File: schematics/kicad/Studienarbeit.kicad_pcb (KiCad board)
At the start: 2 copper layers, 73 x 73 mm, 72 parts, among them J1 AudioJack3, J2 Conn_01x18, J3 Conn_01x18, J4 Conn_01x01_Pin, J5 Conn_01x01_Pin, J6 Conn_01x01_Pin, J7 Conn_01x01_Pin, U2 PCM5102, U3 MCP6001-OT, U4 MCP6001-OT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

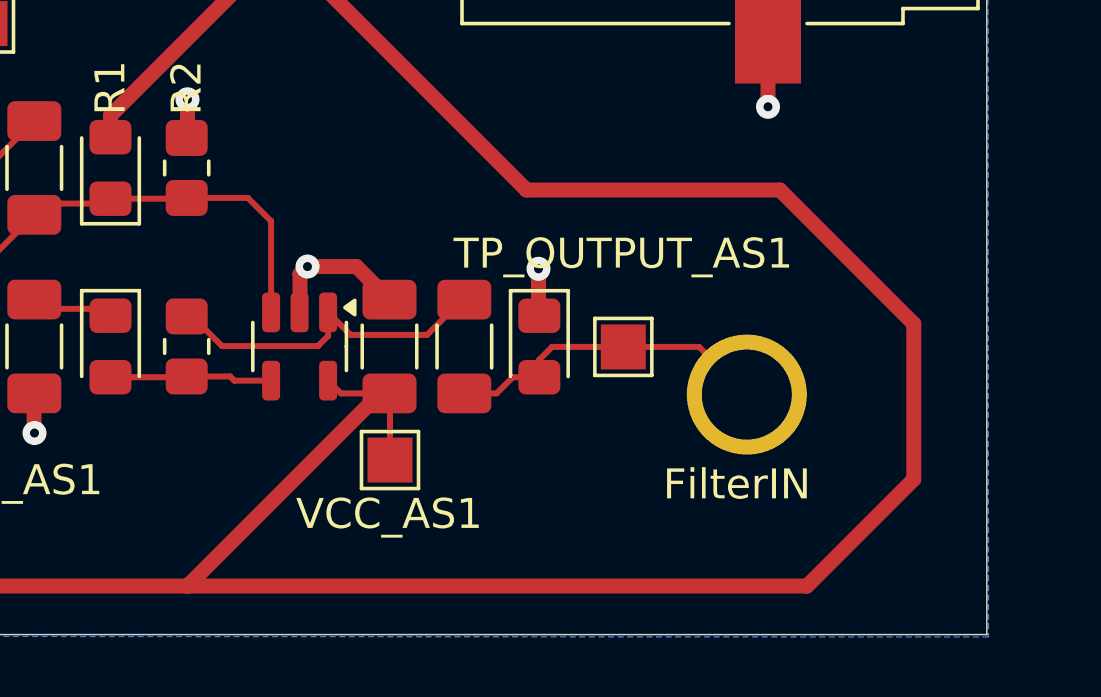
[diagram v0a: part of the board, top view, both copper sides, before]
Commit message: KiCad: Added jumper wires and resistors for gain control.
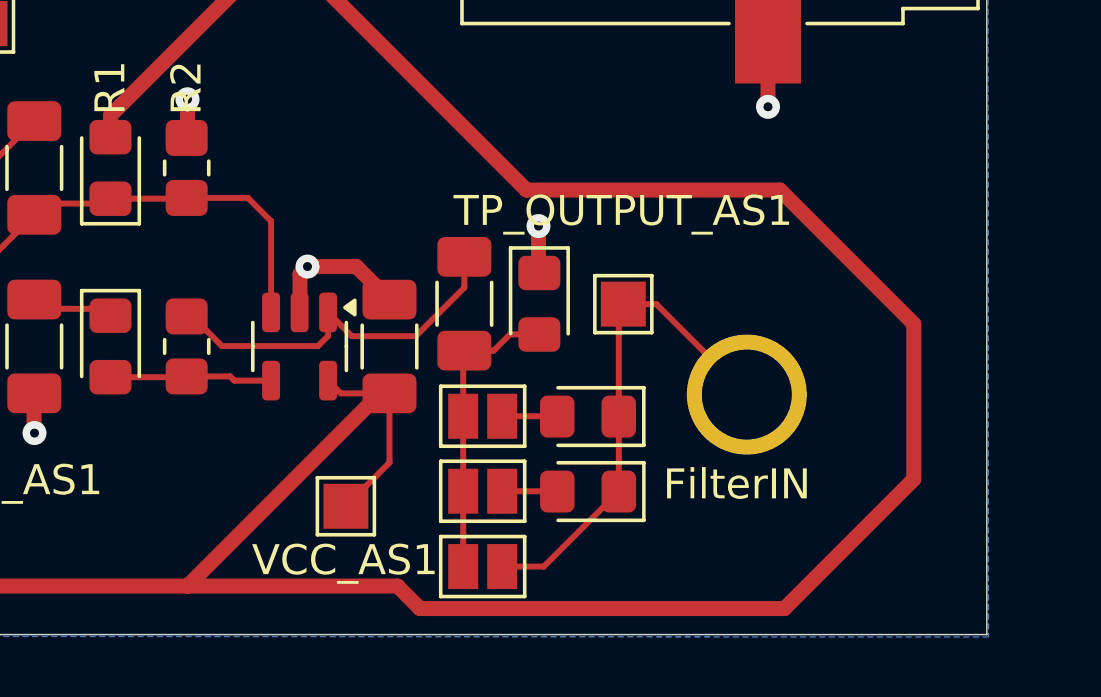
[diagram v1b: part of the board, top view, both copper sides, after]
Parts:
- added JP1: Jumper_2_Open, Jumper:SolderJumper-2_P1.3mm_Open_Pad1.0x1.5mm, F.Cu at (263.8, 104.3)
- added JP2: Jumper_2_Open, Jumper:SolderJumper-2_P1.3mm_Open_Pad1.0x1.5mm, F.Cu at (263.8, 101.8)
- added JP3: Jumper_2_Open, Jumper:SolderJumper-2_P1.3mm_Open_Pad1.0x1.5mm, F.Cu at (263.8, 106.8)
- added R_COUPLING_AMPSTAGE2: 10K, LED_SMD:LED_0805_2012Metric_Pad1.15x1.40mm_HandSolder, F.Cu at (267.3, 104.3)
- added R_COUPLING_AMPSTAGE3: 1K, LED_SMD:LED_0805_2012Metric_Pad1.15x1.40mm_HandSolder, F.Cu at (267.3, 101.8)
- moved VCC_AS1 2.13 mm to (259.2, 104.8)
- moved C_COUPLING_AMPSTAGE1 1.42 mm to (263.2, 98.0)
- moved R_COUPLING_AMPSTAGE1 1.42 mm to (265.7, 98.0)
- moved TP_OUTPUT_AS1 1.42 mm to (268.5, 98.1)
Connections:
- C_COUPLING_AMPSTAGE1 pad 1: /ES2FILTER -> Net-(JP1-A)
- R_COUPLING_AMPSTAGE1 pad 2: /ES2FILTER -> Net-(JP1-A)
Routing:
- net Net-(JP1-A): track 0.00 -> 9.60 mm
- net /ES2FILTER: track 38.3 -> 44.8 mm
- net +5V: track 323.1 -> 325.9 mm
- net Net-(JP1-B): track 0.00 -> 1.84 mm
- net Net-(JP2-B): track 0.00 -> 1.84 mm
- net Net-(C_COUPLING_AMPSTAGE1-Pad2): track 11.3 -> 12.6 mm

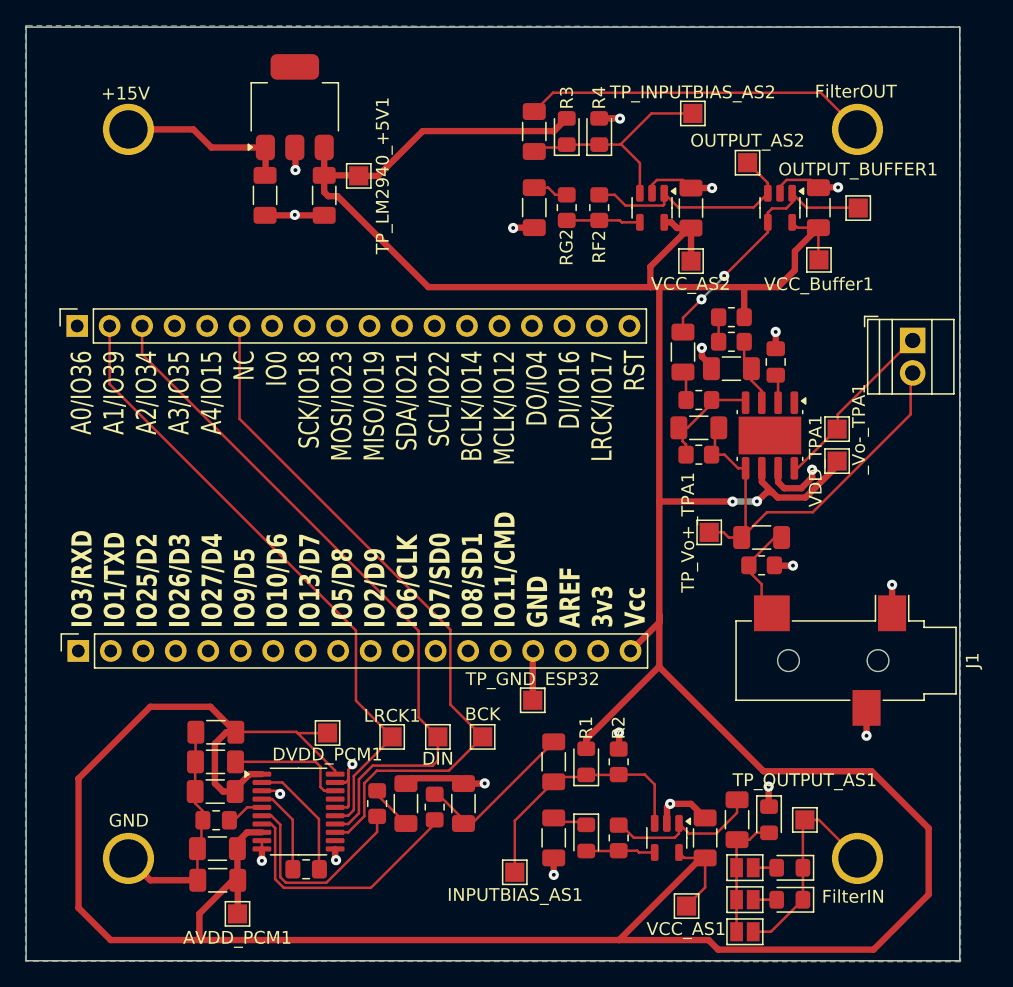
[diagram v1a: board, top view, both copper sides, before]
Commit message: Updated PCB based on feedback (1).
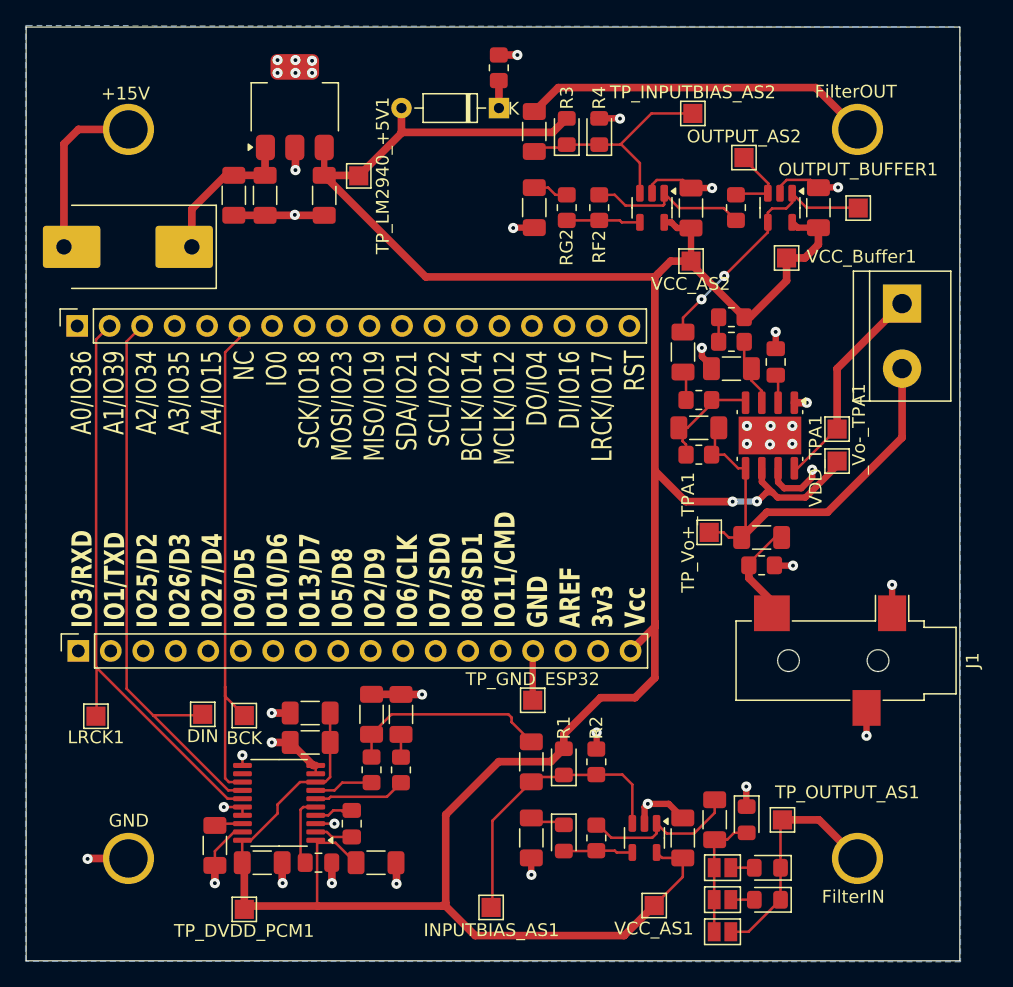
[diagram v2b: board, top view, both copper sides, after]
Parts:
- removed AVDD_PCM1: TestPoint, TestPoint:TestPoint_Pad_1.5x1.5mm
- added C_IN_+15V_1: 10uF, Capacitor_SMD:C_1206_3216Metric_Pad1.33x1.80mm_HandSolder, F.Cu at (223.8, 49.2)
- added D1: D_Schottky, Diode_SMD:D_SMC-RM10_Universal_Handsoldering, F.Cu at (215.6, 53.2)
- added D2: 1N4148, Diode_THT:D_DO-35_SOD27_P7.62mm_Horizontal, F.Cu at (244.6, 42.4)
- added DEBUG1: 0, Resistor_SMD:R_0805_2012Metric_Pad1.20x1.40mm_HandSolder, F.Cu at (263.1, 50.2)
- added STATUS_LED1: 330, Resistor_SMD:R_0805_2012Metric_Pad1.20x1.40mm_HandSolder, F.Cu at (244.6, 39.2)
- LS1: footprint TerminalBlock:TerminalBlock_Xinya_XY308-2.54-2P_1x02_P2.54mm_Horizontal -> TerminalBlock:TerminalBlock_bornier-2_P5.08mm
- moved LRCK1 23.2 mm to (213.1, 90.0), turned to 180 degrees
- moved BCK 18.7 mm to (224.7, 89.9), turned to 0 degrees
- moved DIN 18.5 mm to (221.4, 89.8)
- moved TP_DVDD_PCM1 15.2 mm to (224.7, 105.0)
- moved C1_APS_PCM5102 14.9 mm to (229.8, 89.7)
- moved C1_CPPS_PCM1 13.8 mm to (234.9, 101.4), turned to 180 degrees
- moved C2_APS_PCM5102 11.0 mm to (229.8, 92.0)
- moved C1_DPS_PCM1 10.8 mm to (226.1, 101.4), turned to 180 degrees
- moved CG2_PCM5102 10.0 mm to (234.6, 89.8)
- moved C2_CPPS_PCM1 8.66 mm to (230.4, 101.4), turned to 180 degrees
- moved CG1_PCM5102 6.98 mm to (236.9, 89.8)
- moved C2_DPS_PCM1 6.53 mm to (222.3, 100.0), turned to -90 degrees
- moved ROUTDACR1 5.73 mm to (234.6, 94.1)
- moved CA_PCM5102 5.04 mm to (233.1, 98.3), turned to 90 degrees
- moved INPUTBIAS_AS1 3.31 mm to (243.9, 104.9)
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- renumbered DVDD_PCM1 to TP_DVDD_PCM1
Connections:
- C_INPUT_LDO1 pad 2: +15V -> Net-(D1-K)
- C_IN_AMPSTAGE1 pad 1: /ES2FILTER -> /Filter_OUT
- J6 pad 1: /ES2FILTER -> /Filter_OUT
- J7 pad 1: /ES2FILTER -> /Filter_IN
- JP3 pad 2: /ES2FILTER -> /Filter_IN
- OUTPUT_AS2 pad 1: Net-(RF2-Pad2) -> Net-(DEBUG1-Pad2)
- RF2 pad 2: Net-(RF2-Pad2) -> Net-(DEBUG1-Pad1)
- R_COUPLING_AMPSTAGE2 pad 1: /ES2FILTER -> /Filter_IN
- R_COUPLING_AMPSTAGE3 pad 1: /ES2FILTER -> /Filter_IN
- TP_OUTPUT_AS1 pad 1: /ES2FILTER -> /Filter_IN
- U2 pad 12: /SCK -> unconnected-(U2-SCK-Pad12)
- U2 pad 17: /XSMT/MUTE -> GND
- U3 pad 1: Net-(RF2-Pad2) -> Net-(DEBUG1-Pad1)
- U5 pad 3: Net-(RF2-Pad2) -> Net-(DEBUG1-Pad2)
- U6 pad 1: /SYSTEMCTL -> GND
- U7 pad 1: +15V -> Net-(D1-K)
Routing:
- net +5V: track 325.9 -> 234.5 mm
- net /ES2FILTER: track 44.8 -> 0.00 mm
- net /Filter_OUT: track 0.00 -> 27.5 mm
- net /Filter_IN: track 0.00 -> 19.4 mm
- net Net-(RF2-Pad2): track 18.4 -> 0.00 mm
- net /BCK: track 56.1 -> 40.2 mm
- net Net-(U2-OUTR): track 20.3 -> 4.62 mm
- net Net-(DEBUG1-Pad1): track 0.00 -> 12.8 mm
- net Net-(D1-K): track 0.00 -> 12.0 mm
- net /DIN: track 55.2 -> 45.1 mm
- net Net-(U2-OUTL): track 16.4 -> 7.59 mm
- net /LDOO: track 9.62 -> 2.31 mm
- net Net-(U2-CAPP): track 9.59 -> 3.06 mm
- net Net-(DEBUG1-Pad2): track 0.00 -> 5.60 mm
- net GND: track 88.4 -> 84.7 mm, vias 21 -> 35
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
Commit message: Updated the PCB with prof feedback.
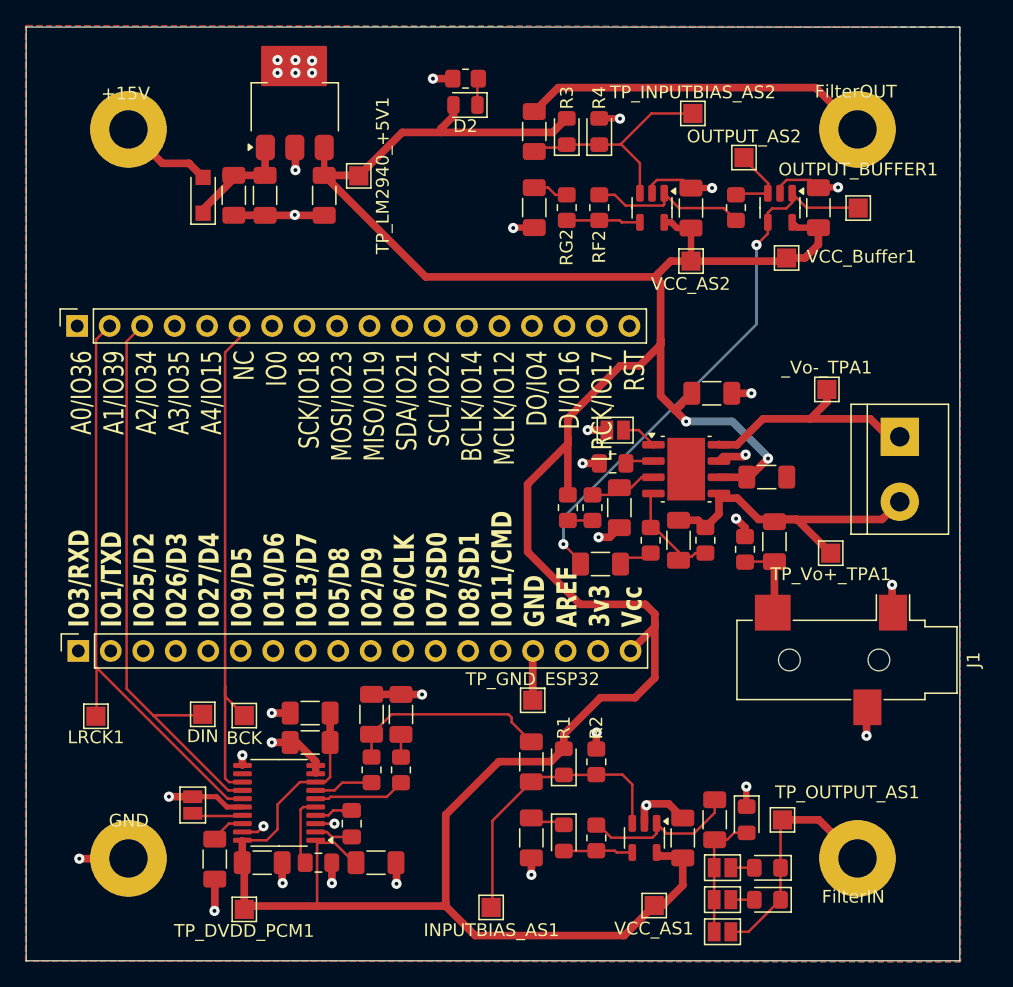
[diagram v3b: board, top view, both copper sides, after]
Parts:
- removed VDD_TPA1: TestPoint, TestPoint:TestPoint_Pad_1.5x1.5mm
- added C_INPUT_TPA1: 10uF, Capacitor_SMD:C_1206_3216Metric_Pad1.33x1.80mm_HandSolder, F.Cu at (265.5, 71.2)
- added C_INPUT_TPA2: 100nF, Capacitor_SMD:C_1206_3216Metric_Pad1.33x1.80mm_HandSolder, F.Cu at (261.2, 64.7)
- added JP4: Jumper_2_Open, Jumper:SolderJumper-2_P1.3mm_Open_Pad1.0x1.5mm, F.Cu at (220.6, 96.9)
- added JP5: Jumper_2_Open, Jumper:SolderJumper-2_P1.3mm_Open_Pad1.0x1.5mm, F.Cu at (253.7, 67.6)
- D1: footprint Diode_SMD:D_SMC-RM10_Universal_Handsoldering -> Diode_SMD:Nexperia_CFP3_SOD-123W
- D2: footprint Diode_THT:D_DO-35_SOD27_P7.62mm_Horizontal -> Diode_SMD:D_0805_2012Metric
- J4, J5, J6, J7: footprint TestPoint:TestPoint_THTPad_2.0x2.0mm_Drill1.0mm -> TestPoint:FestoBoard_Drill_Hole
- moved R12 19.6 mm to (249.9, 73.6), turned to 90 degrees
- moved CI_TPA711 17.8 mm to (252.5, 78.0), turned to 180 degrees
- moved R13 16.9 mm to (251.9, 73.6), turned to 90 degrees
- moved CB_TPA1 15.0 mm to (253.4, 70.2), turned to 180 degrees
- moved C_SE/BTL_TPA1 14.0 mm to (254.0, 73.6), turned to -90 degrees
- moved RI_TPA711 11.6 mm to (256.4, 76.2), turned to 90 degrees
- moved LS1 10.4 mm to (275.9, 68.1)
- moved TP_Vo+_TPA1 9.64 mm to (270.5, 77.2), turned to 180 degrees
- moved CF_TPA711 8.93 mm to (258.6, 76.2), turned to 90 degrees
- moved D1 7.13 mm to (221.4, 49.2), turned to 90 degrees
- moved U6 7.06 mm to (259.2, 70.6), turned to 0 degrees
- moved RF_TPA711 6.71 mm to (260.7, 76.2), turned to -90 degrees
- moved _Vo-_TPA1 3.20 mm to (270.2, 64.4), turned to 180 degrees
- moved STATUS_LED1 2.74 mm to (241.9, 40.1), turned to 0 degrees
- moved D2 2.63 mm to (241.9, 42.2)
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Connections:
- U2 pad 17: GND -> Net-(JP4-B)
- U6 pad 1: GND -> Net-(JP5-B)
- U7 pad 4: (no net) -> GND
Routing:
- net /BUFFEROUT: track 20.7 -> 43.2 mm
- net +5V: track 234.5 -> 250.2 mm
- net /Vo+: track 35.2 -> 25.6 mm
- net GND: track 84.7 -> 91.0 mm, vias 35 -> 37
- net +15V: track 13.6 -> 7.39 mm
- net Net-(JP4-B): track 0.00 -> 4.35 mm
- net /Vo-: track 16.6 -> 19.5 mm
- net Net-(JP5-B): track 0.00 -> 2.82 mm
- net Net-(D1-K): track 12.0 -> 9.31 mm
- net Net-(CC_TPA711-Pad2): track 10.4 -> 8.44 mm
- net unconnected-(U6-GND-Pad9): vias 6 -> 0
- added copper zone on F.Cu, net GND

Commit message: Updated the parts list.
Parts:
- D1: footprint Diode_SMD:Nexperia_CFP3_SOD-123W -> Diode_SMD:D_SOD-123F
- D2: footprint Diode_SMD:D_0805_2012Metric -> Diode_SMD:D_SOD-123F
- RF1, RF2: value 10K -> 5K
- RG1: value 200k -> 100k; footprint LED_SMD:LED_0805_2012Metric_Pad1.15x1.40mm_HandSolder -> Resistor_SMD:R_0805_2012Metric_Pad1.20x1.40mm_HandSolder
- RG2: value 200K -> 100K
- R_COUPLING_AMPSTAGE1: footprint LED_SMD:LED_0805_2012Metric_Pad1.15x1.40mm_HandSolder -> Resistor_SMD:R_0805_2012Metric_Pad1.20x1.40mm_HandSolder
- moved D2 0.14 mm to (241.8, 42.2)
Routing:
- net GND: vias 37 -> 38

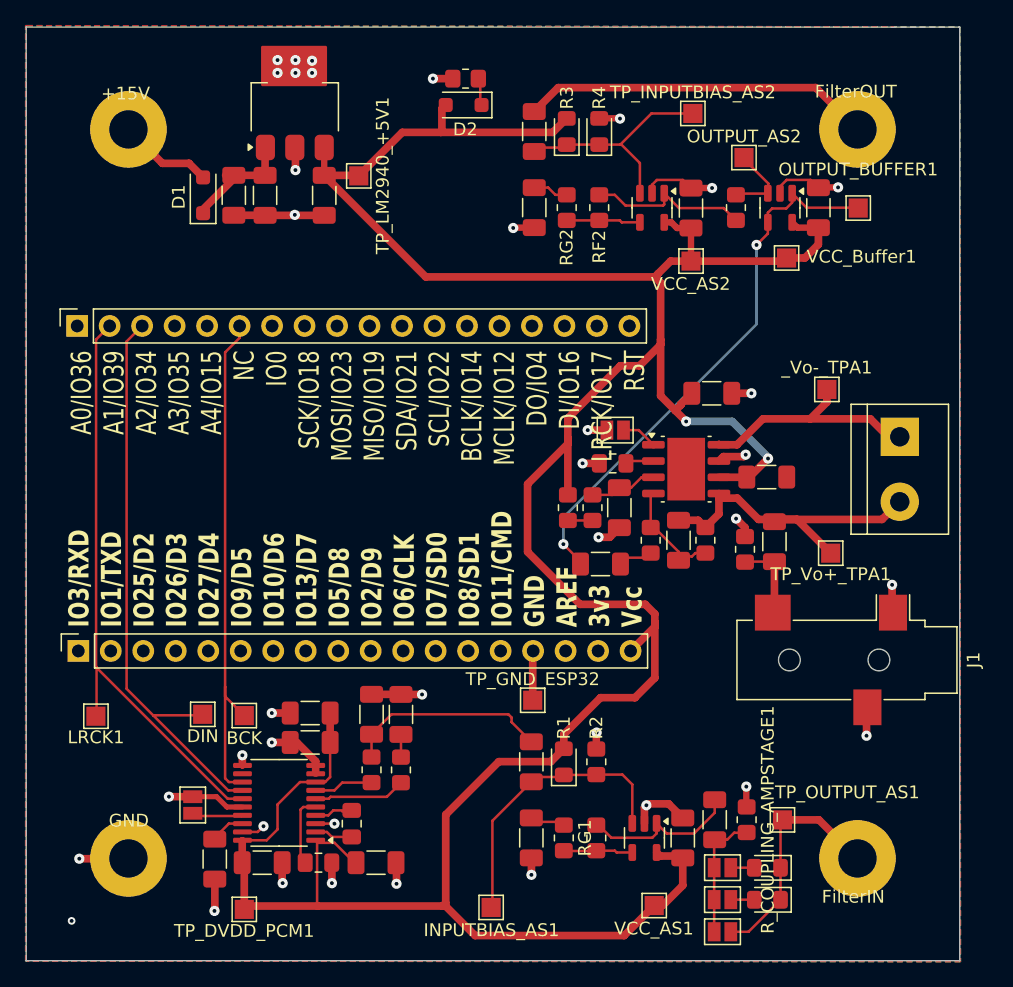
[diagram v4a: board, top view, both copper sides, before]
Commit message: Updated the audio jack to a switching jack.
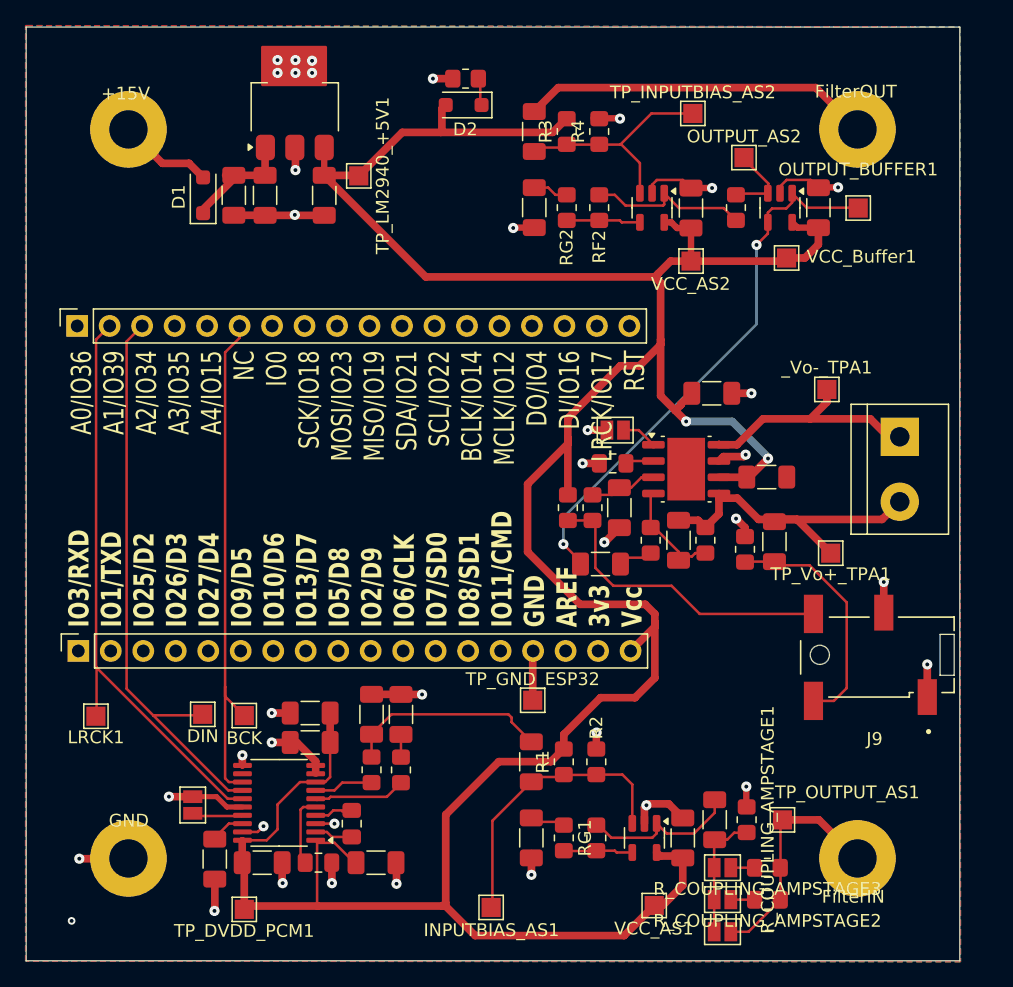
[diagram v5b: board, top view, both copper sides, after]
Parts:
- removed J1: AudioJack3, Connector_Audio:Jack_3.5mm_CUI_SJ-3523-SMT_Horizontal
- added J9: SJ2-35853B-SMT-TR, SJ2-35853B-SMT-TR:CUI_SJ2-35853B-SMT-TR, F.Cu at (274.1, 85.2)
- R1, R3, R4, R_COUPLING_AMPSTAGE2, R_COUPLING_AMPSTAGE3: footprint LED_SMD:LED_0805_2012Metric_Pad1.15x1.40mm_HandSolder -> Resistor_SMD:R_0805_2012Metric_Pad1.20x1.40mm_HandSolder
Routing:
- net /SE/~{BTL}_SWITCH: track 1.93 -> 24.3 mm
- net Net-(CC_TPA711-Pad2): track 8.44 -> 19.0 mm
